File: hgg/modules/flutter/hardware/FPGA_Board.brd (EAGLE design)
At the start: 100 x 77 mm, 85 parts, among them IC1 AT45DB161D-SU, IC2 MEGA8-AI, IC3 MAX481CSA, Q1 8Mhz, U2 XC3S50AVQ100, X1 BU-SMA-V, X2 MINI-USB-32005-201

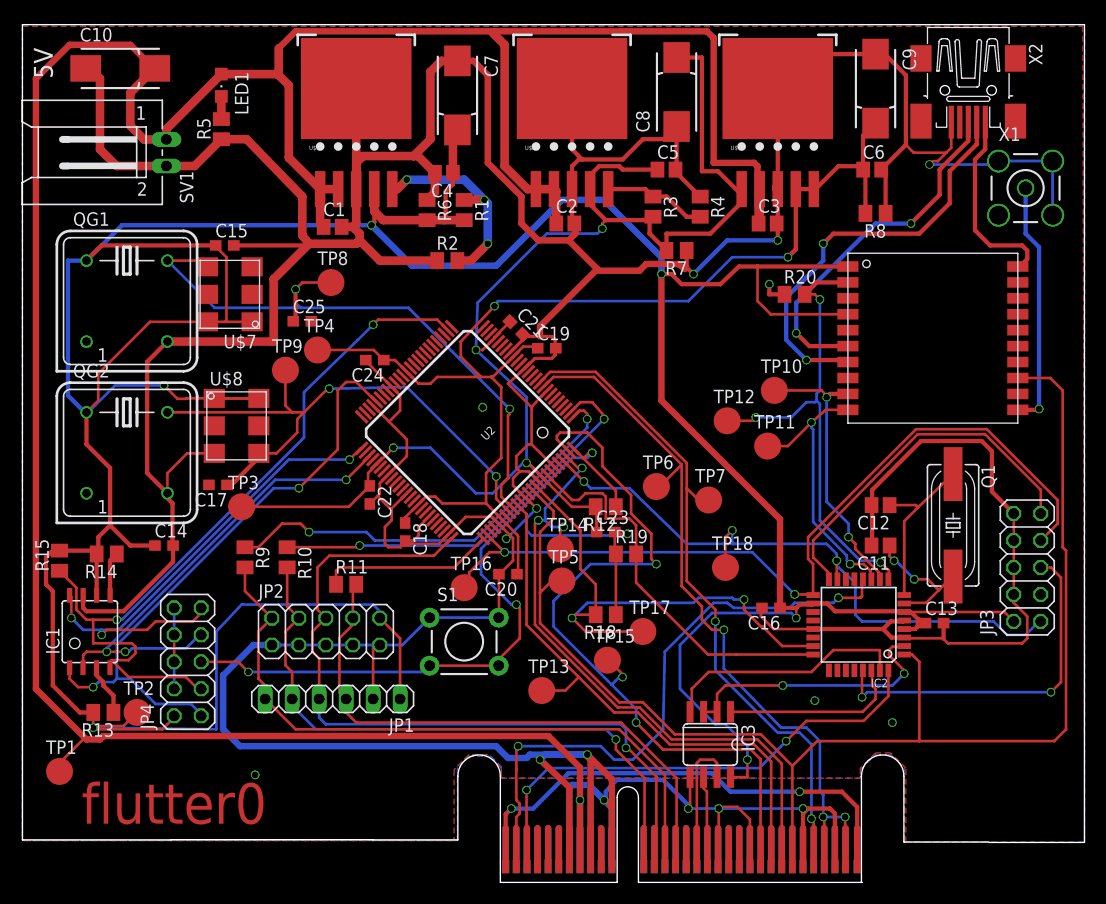
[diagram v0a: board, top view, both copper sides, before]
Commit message: changed package of resistors and capasitors to 0603 added values
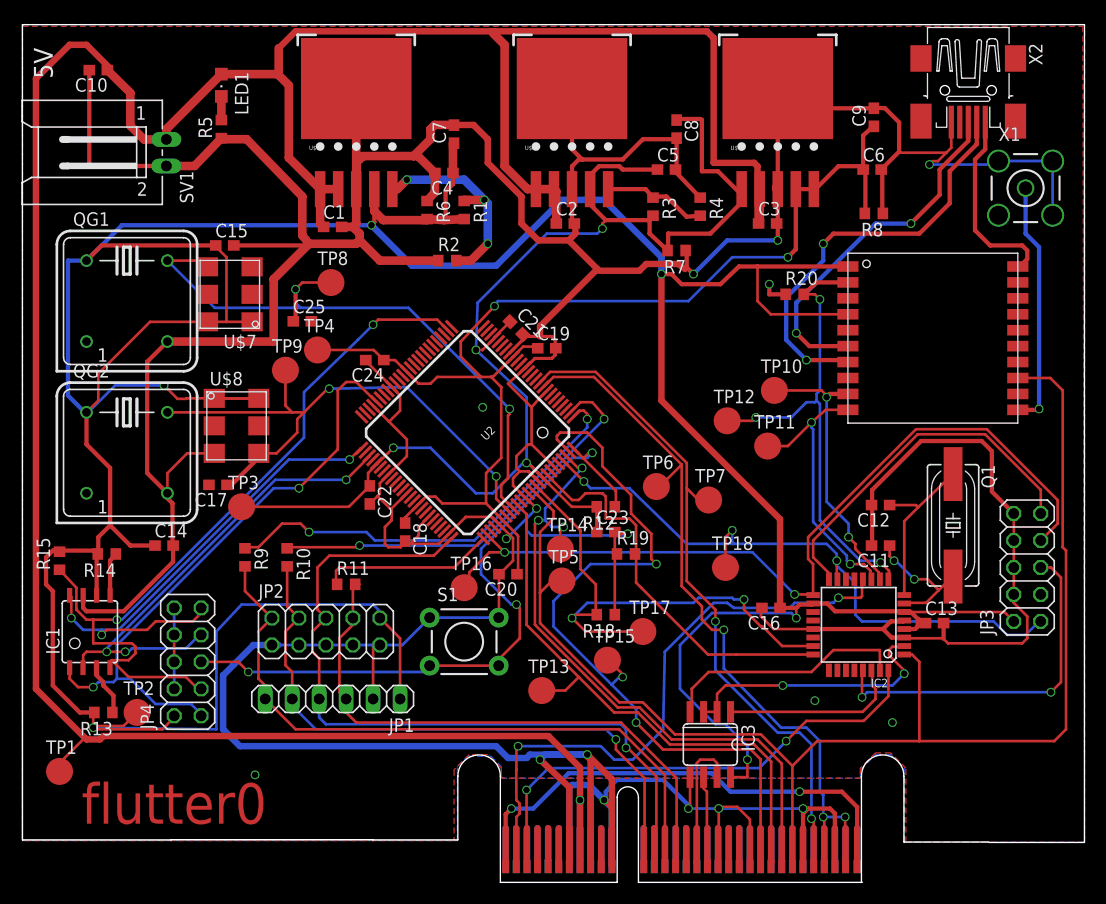
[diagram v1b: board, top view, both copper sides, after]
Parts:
- C1, C2, C3, C4, C5, C6: value (none) -> 100n; device resistor:C0805 -> resistor:C0603
- C10, C7, C8, C9: value (none) -> 10u; device resistor:085CS_1AR -> resistor:C0603
- C11, C12: device resistor:C0805 -> resistor:C0603
- C13, C14, C15, C16, C18, C19, C20, C21, C22, C23, C24: value (none) -> 100n
- C17, C25: value (none) -> 15p
- R1, R13, R14, R15, R18, R19, R2, R20, R3, R4, R5, R6, R7, R8: device resistor:M0805 -> resistor:R0603
- R10, R11, R9: value (none) -> 68; device resistor:M0805 -> resistor:R0603
- R12: value (none) -> 4.7k; device resistor:M0805 -> resistor:R0603
- moved C7 3.67 mm to (40.6, 69.7), turned to 90 degrees
- moved C8 3.49 mm to (61.6, 70.2), turned to 270 degrees
- moved C9 2.70 mm to (80.2, 71.3), turned to 90 degrees
- moved C10 2.07 mm to (7.14, 75.7), turned to 180 degrees
- moved R8 0.16 mm to (80.2, 62.2)
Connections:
- net +5V: now also C10.1; no longer C10.+
- net GND: now also C10.2, C7.2, C8.2, C9.2; no longer C10.-, C7.-, C8.-, C9.-
- net VCC1.2: now also C9.1; no longer C9.+
- net VCC2.5: now also C8.1; no longer C8.+
- net VCC3.3: now also C7.1; no longer C7.+
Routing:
- net GND: track 715.7 -> 699.1 mm
- net VCC2.5: track 132.2 -> 126.5 mm
- net +5V: track 279.0 -> 274.1 mm
- net VCC3.3: track 405.1 -> 404.3 mm

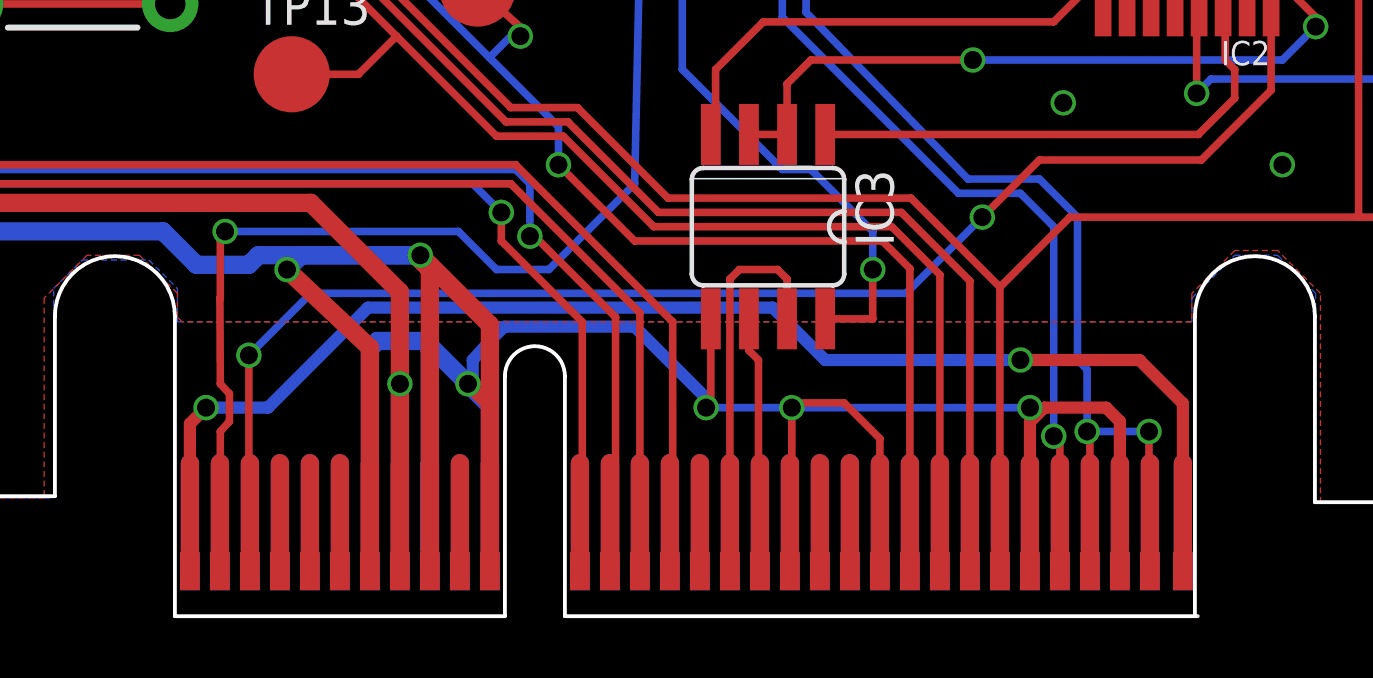
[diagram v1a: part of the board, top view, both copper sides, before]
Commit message: fixed issue #27: moved signals to the other side of friendship connector
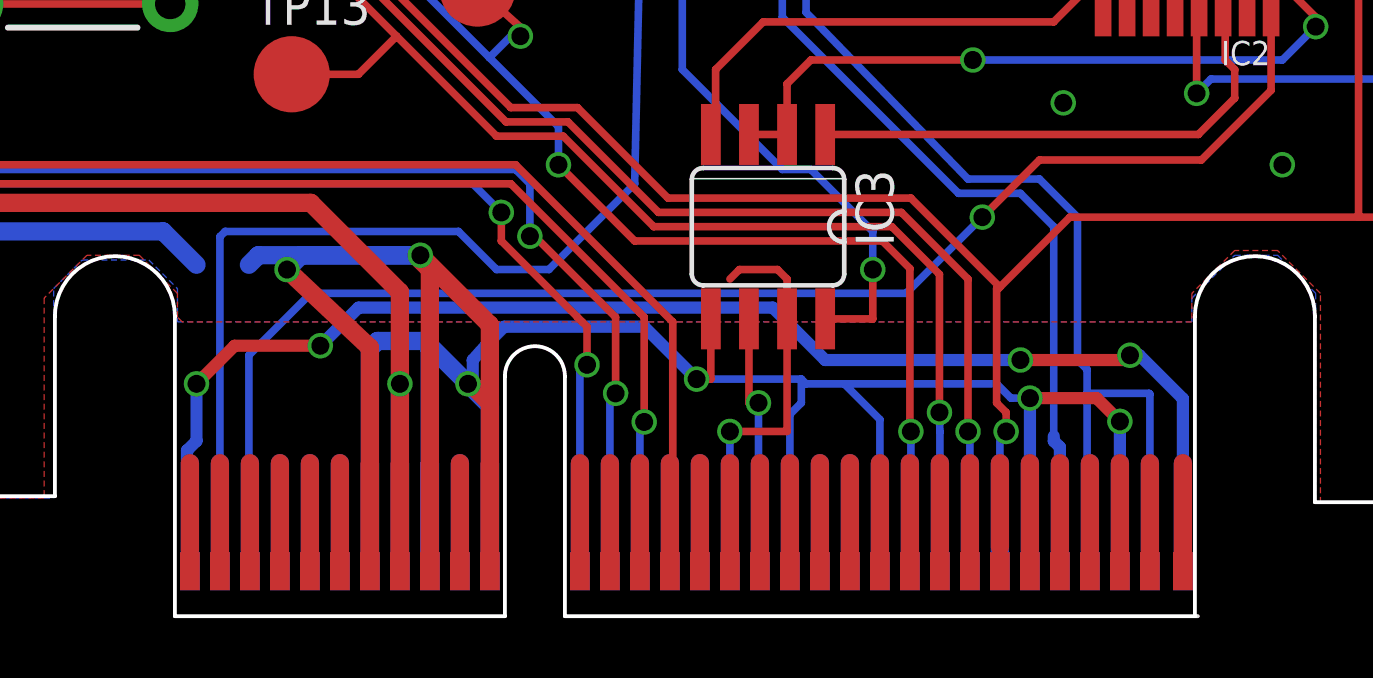
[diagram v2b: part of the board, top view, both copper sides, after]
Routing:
- net GND: track 699.1 -> 696.6 mm
- net FASTCLK+: track 72.2 -> 73.6 mm, vias 3 -> 1
- net N$13: track 46.5 -> 47.5 mm, vias 2 -> 4
- net BUS0-: track 13.2 -> 13.8 mm, vias 0 -> 1
- net PPS: track 128.4 -> 128.7 mm, vias 0 -> 1
- net IRQ: track 57.0 -> 56.8 mm, vias 2 -> 1
- net BUS0+: track 8.56 -> 8.75 mm, vias 0 -> 1
- net CS: track 47.4 -> 47.5 mm, vias 2 -> 1
- net TDI: track 59.3 -> 59.4 mm, vias 1 -> 2
- net TMS: track 63.5 -> 63.7 mm, vias 0 -> 1
- net SLOWCLK/MOSI: vias 3 -> 4
- net SLOWCLK/CLK: vias 0 -> 1
- net TDO: vias 1 -> 2
- net SLOWCLK/CS: vias 3 -> 4
- net FASTCLK-: vias 2 -> 1

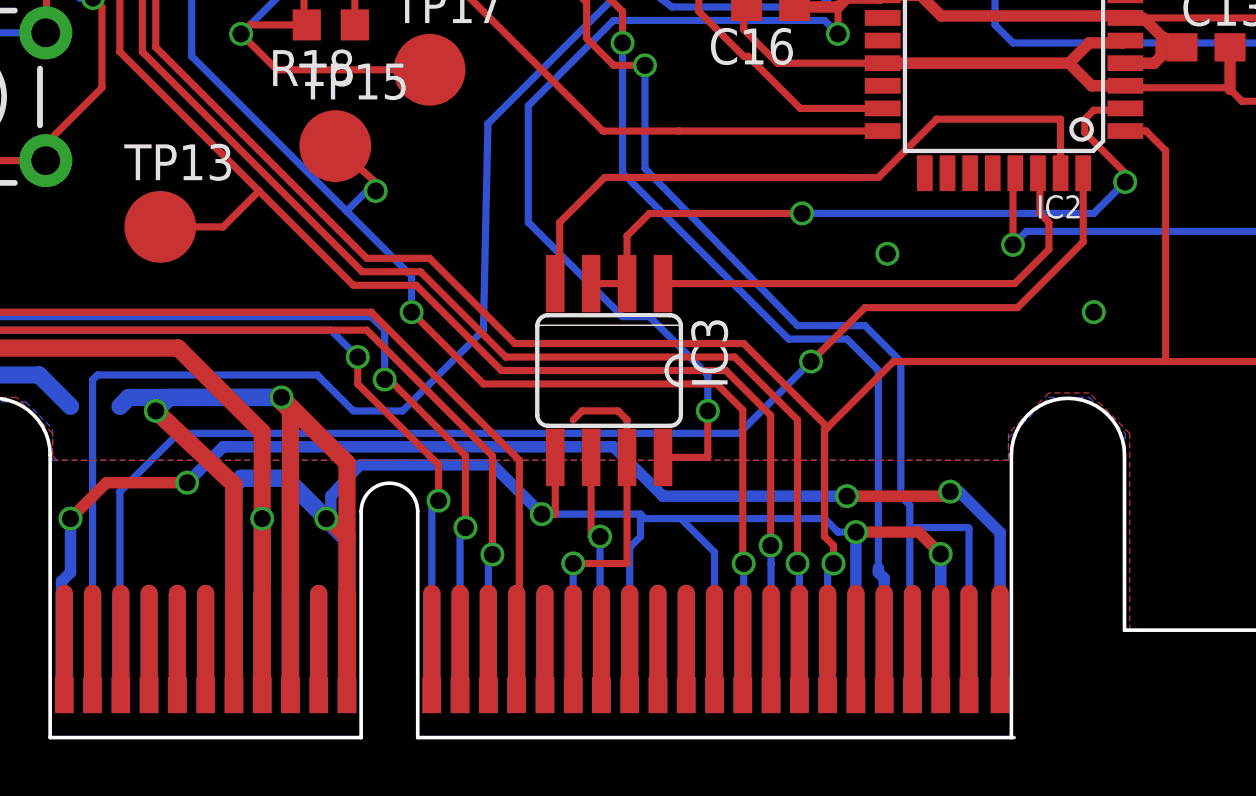
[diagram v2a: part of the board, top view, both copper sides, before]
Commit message: changed supply of rs485 transciever to 5V
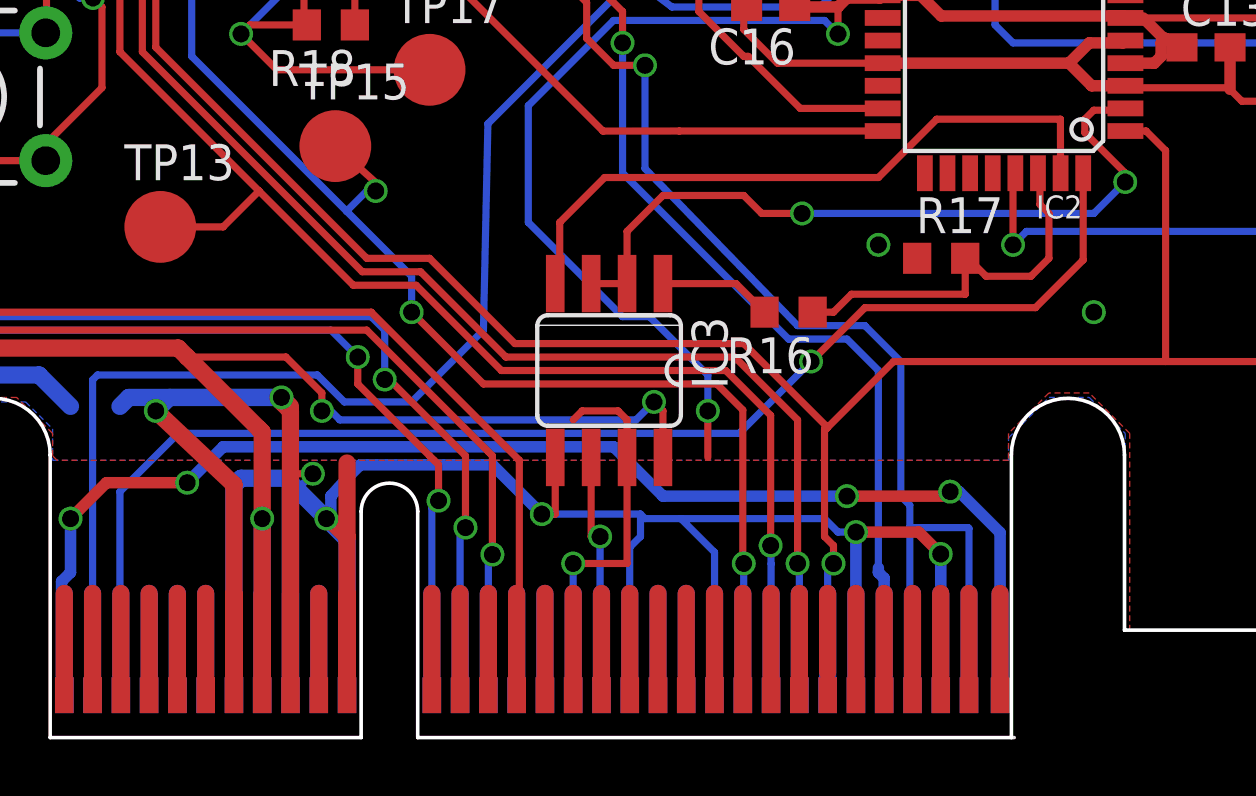
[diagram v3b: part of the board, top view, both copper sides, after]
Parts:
- added R16: 1k, resistor:R0603
- added R17: 1.6k, resistor:R0603
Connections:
- removed net DO: IC2.30, IC3.1
- new net N$6: IC2.30, R16.1, R17.2
- new net N$9: IC3.1, R16.2
- net +5V: now also IC3.8
- net GND: now also R17.1
- net VCC3.3: no longer IC3.8
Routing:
- net GND: track 696.6 -> 718.4 mm, vias 17 -> 18
- net +5V: track 274.1 -> 294.9 mm, vias 1 -> 3
- net DO: track 17.0 -> 0.00 mm
- net N$6: track 0.00 -> 13.7 mm
- net N$9: track 0.00 -> 4.12 mm
- net VCC3.3: track 404.3 -> 402.7 mm
- net N$5: track 25.8 -> 26.4 mm
